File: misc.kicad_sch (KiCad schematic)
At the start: 0 parts

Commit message: [#56643] Create buses for interfaces, assign buses to blocks
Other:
- company: (none) -> Antmicro Ltd.
- title: (none) -> Com Express 7 baseboard
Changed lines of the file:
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@@
 (kicad_sch (version 20230121) (generator eeschema)
-  (paper "A4")
+  (paper "A3")
+  (title_block
+    (title "Com Express 7 baseboard")
+    (date "2024-03-22")
+    (rev "1.0.0")
+    (company "Antmicro Ltd.")
+  )
 )

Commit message: [#57905] Add ADT7476AARQZ temperature/voltage/fan system monitor, LEDs
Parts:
- added C135, C137, C138, C139, C140, C141, C142, C143, C144: C_100n_0402, antmicro-footprints:C_0402_1005Metric, symbol antmicroCapacitors0402:C_100n_0402
- added C136: C_10u_0402, antmicro-footprints:C_0402_1005Metric, symbol antmicroCapacitors0402:C_10u_0402
- added D19: LED_RGB_PLCC4_ASMB_MTB1_0A3A2, antmicro-footprints:PLCC4_3.2x2.8mm, symbol antmicroLEDIndicationDiscrete:LED_RGB_PLCC4_ASMB_MTB1_0A3A2
- added D20: LED_G_0603_LTST-C190GKT, antmicro-footprints:LED_0603_1608Metric_G, symbol antmicroLEDIndicationDiscrete:LED_G_0603_LTST-C190GKT
- added F1: PTC_3A_1210, antmicro-footprints:F_1210_3225Metric, symbol antmicroFuses:PTC_3A_1210
- added H4, H5: Lightpipe_Bivar_SLP3-300-250-F, antmicro-footprints:Mech_Lightpipe_Bivar_SLP3-300-250-F, symbol antmicroMechanicalParts:Lightpipe_Bivar_SLP3-300-250-F
- added J10, J11, J12: Molex_KK_1x4_0470531000, antmicro-footprints:Conn_Molex_KK_1x4_0470531000, symbol antmicroWire2BoardConnectors:Molex_KK_1x4_0470531000
- added Q3, Q4: MMBT3904LT1G, antmicro-footprints:SOT-23-3, symbol antmicroTransistorsBipolarSingle:MMBT3904LT1G
- added R241, R242, R247: R_0R_0402, antmicro-footprints:R_0402_1005Metric, symbol antmicroResistors0402:R_0R_0402
- added R243, R244, R245, R246: R_10k_0402, antmicro-footprints:R_0402_1005Metric, symbol antmicroResistors0402:R_10k_0402
- added R248, R249, R250: R_220R_0402, antmicro-footprints:R_0402_1005Metric, symbol antmicroResistors0402:R_220R_0402
- added R251: R_330R_0402, antmicro-footprints:R_0402_1005Metric, symbol antmicroResistors0402:R_330R_0402
- added TP71, TP72, TP73, TP74, TP75: TP_0.75mm_SMD, antmicro-footprints:TP_SMD_0.75mm, symbol antmicroTestPoints:TP_0.75mm_SMD
- added U36: ADT7476AARQZ, symbol antmicroTemperatureSensorsAnalogandDigitalOutput:ADT7476AARQZ
- added U37, U38, U39: NTS0102_TSSOP, antmicro-footprints:TSSOP-8_3x3mm_P0.65mm, symbol antmicroLogicTranslatorsLevelShifters:NTS0102_TSSOP
- added U40, U41: 74LVC1G157-Q100H_SOT457, antmicro-footprints:SC-74-6_1.5x2.9mm_P0.95mm, symbol antmicroInterfaceAnalogSwitchesMultiplexersDemultiplexers:74LVC1G157-Q100H_SOT4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
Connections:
- new net: R241.2, U36.20 (+5V_{IN})
- new net: TP71.1, U36.8 (GPIO3)
- new net: D19.2 (C_{G}), R249.2
- new net: TP74.1, U36.5 (GPIO0)
- new net: R242.2, U36.21 (+12V_{IN})
- new net: Q4.1 (B), Q4.3 (C), U36.18 (D1+)
- new net: Q4.2 (E), U36.17 (D1-)
- new net: TP73.1, U36.6 (GPIO1)
- new net: D19.1 (C_{R}), R251.2
- new net: Q3.2 (E), U36.15 (D2-)
- new net: Q3.1 (B), Q3.3 (C), U36.16 (D2+)
- new net: R247.1, U36.19 (GPIO4)
- new net: TP72.1, U36.7 (GPIO2)
- new net: TP75.1, U36.9 (TACH3)
- new net: D20.1, R248.1
- new net: D19.3 (C_{B}), R250.2
- new net +12V: F1.1, R242.1
- new net +3V3: C135.2, C138.2, C139.2, C141.2, C143.2, C144.2, R243.2, R244.2, R246.2, R248.2, U36.4 (VCC), U37.3 (VCC_{A}), U37.6 (OE), U38.3 (VCC_{A}), U38.6 (OE), U39.3 (VCC_{A}), U39.6 (OE), U40.5 (VCC), U41.5 (VCC)
- new net +5V: C137.2, C140.2, C142.2, D19.4 (A), R241.1, U37.7 (VCC_{B}), U38.7 (VCC_{B}), U39.7 (VCC_{B})
- new net FAN_12V: C136.2, F1.2, J10.2, J11.2, J12.2
- new net GND: C135.1, C136.1, C137.1, C138.1, C139.1, C140.1, C141.1, C142.1, C143.1, C144.1, D20.2, J10.1, J11.1, J12.1, R245.1, U36.3 (GND), U37.2 (GND), U38.2 (GND), U39.2 (GND), U40.2 (GND), U41.2 (GND)
- new net LED_B: R250.1
- new net LED_G: R249.1
- new net LED_R: R251.1
- new net PWM1: U36.24 (PWM1/XTO), U40.3 (I0)
- new net PWM2: U36.10 (PWM2/~{SMB_{ALERT}}), U41.3 (I0)
- new net PWM_{A3V3}: U37.4 (A_{2}), U40.4 (Y)
- new net PWM_{A5V}: J12.4, U37.1 (B_{2})
- new net PWM_{B3V3}: U38.4 (A_{2}), U41.4 (Y)
- new net PWM_{B5V}: J10.4, U38.1 (B_{2})
- new net PWM_{C5V}: J11.4, U39.1 (B_{2})
- new net PWM_{CPUFAN}: U39.4 (A_{2}), U40.1 (I1), U41.1 (I1)
- new net PWM_{SRCSEL}: R246.1, R247.2, U40.6 (S), U41.6 (S)
- new net SMBus.SCL: U36.2 (SCL)
- new net SMBus.SDA: U36.1 (SDA)
- new net TACH_{A3V3}: U36.11 (TACH1), U37.5 (A_{1})
- new net TACH_{A5V}: J12.3, U37.8 (B_{1})
- new net TACH_{B3V3}: U36.12 (TACH2), U38.5 (A_{1})
- new net TACH_{B5V}: J10.3, U38.8 (B_{1})
- new net TACH_{C5V}: J11.3, U39.8 (B_{1})
- new net TACH_{CPUFAN}: U39.5 (A_{1})
- new net ~{ADDREN}: R243.1, U36.13 (PWM3/~{ADDREN})
- new net ~{ADDRSEL}: R244.1, R245.2, U36.14 (TACH4/~{ADDR_{SEL}}/GPIO6)
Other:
- note added: "Boot LED"
- note added: "CASE FAN #1"
- note added: "CASE FAN #2"
- note added: "CPU FAN"
- note added: "Case fans can either share PWM speed control with CPU fan or be individually controlled from ADT7476AARQZ |PWM_{SRCSEL}| SOURCE | |0 | ADT7476 | |1 | CPU_{PWM} | It's high by default"
- note added: "Cold side temperature sensor"
- note added: "FAN CONNECTORS"
- note added: "FAN/VOLTAGE/TEMPERATURE MONITOR"
- note added: "FRONT PANEL LEDS"
- note added: "Hot side temperature sensor"
- note added: "Status LED"

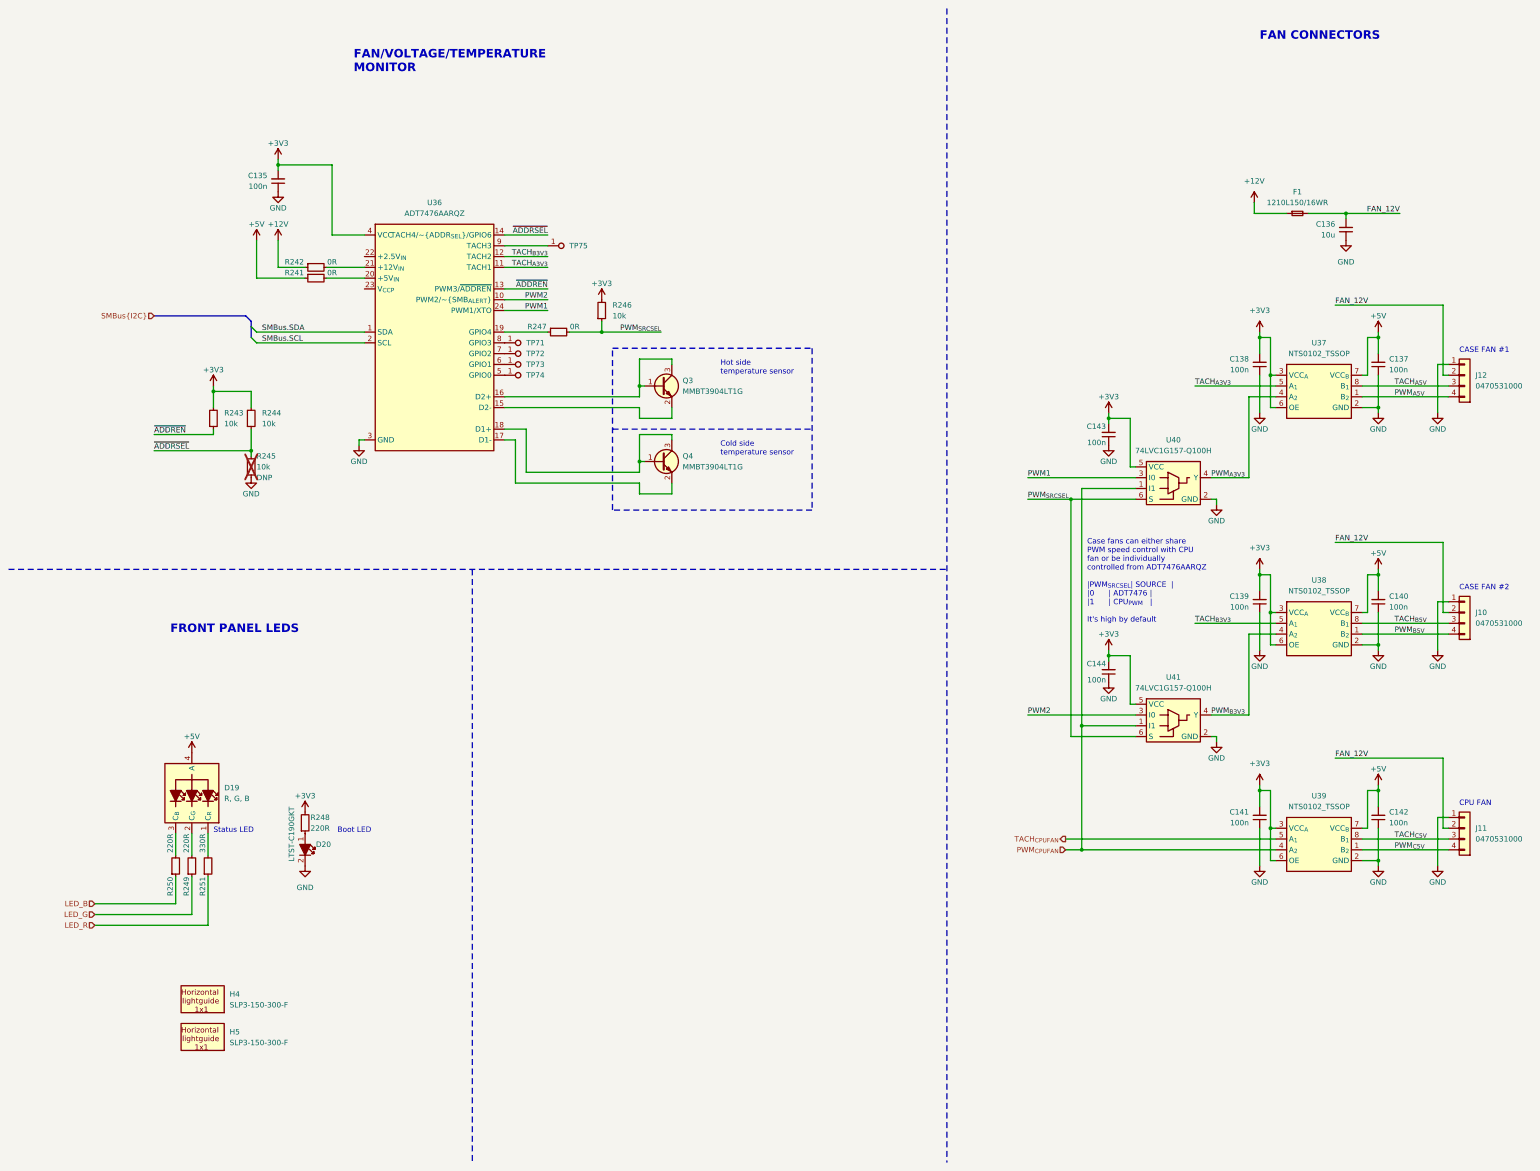
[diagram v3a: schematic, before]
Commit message: [#58137] Update backplane connector pinout
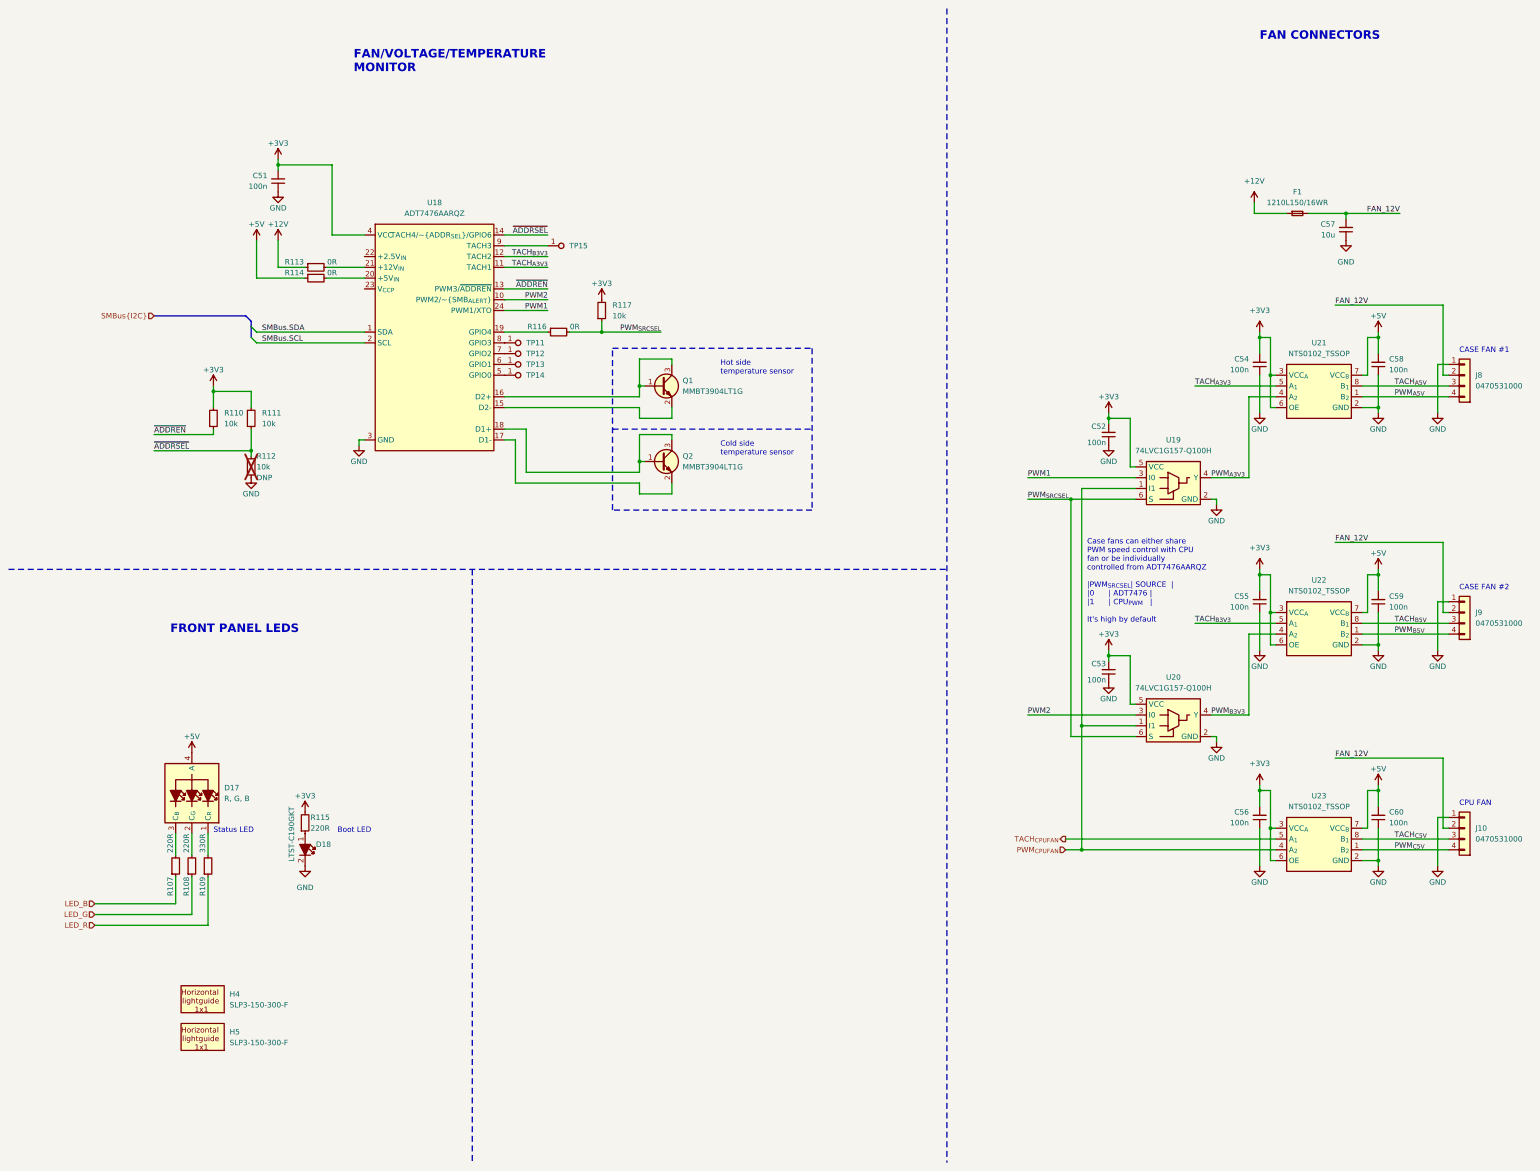
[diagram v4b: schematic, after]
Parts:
- renumbered C135 to C51, C143 to C52, C144 to C53, C138 to C54, C139 to C55, C141 to C56, C136 to C57, C137 to C58, C140 to C59, C142 to C60, D19 to D17, D20 to D18, J11 to J10, J12 to J8, J10 to J9, Q3 to Q1, Q4 to Q2, R250 to R107, R249 to R108, R251 to R109, R243 to R110, R244 to R111, R245 to R112, R242 to R113, R241 to R114, R248 to R115, R247 to R116, R246 to R117, TP71 to TP11, TP72 to TP12, TP73 to TP13, TP74 to TP14, TP75 to TP15, U36 to U18, U40 to U19, U41 to U20, U37 to U21, U38 to U22, U39 to U23

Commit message: Update symbols from the library
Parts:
- U18: footprint (none) -> antmicro-footprints:QSOP-24_8.65x6mm_P0.635mm; Author (none) -> Antmicro; License (none) -> Apache-2.0
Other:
- moved on the sheet: U18
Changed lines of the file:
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@@
       (effects (font (size 1.27 1.27)) hide)
     )
-    (property "Footprint" "" (at 96.52 66.04 0)
+    (property "Footprint" "antmicro-footprints:QSOP-24_8.65x6mm_P0.635mm" (at 96.52 66.04 0)
       (effects (font (size 1.27 1.27)) hide)
     )
@@
       (effects (font (size 1.27 1.27)) hide)
     )
+    (property "Author" "Antmicro" (at 144.78 83.82 0)
+      (effects (font (size 1.27 1.27) (thickness 0.15)) (justify left bottom) hide)
+    )
+    (property "License" "Apache-2.0" (at 144.78 86.36 0)
+      (effects (font (size 1.27 1.27) (thickness 0.15)) (justify left bottom) hide)
+    )
     (pin "5")

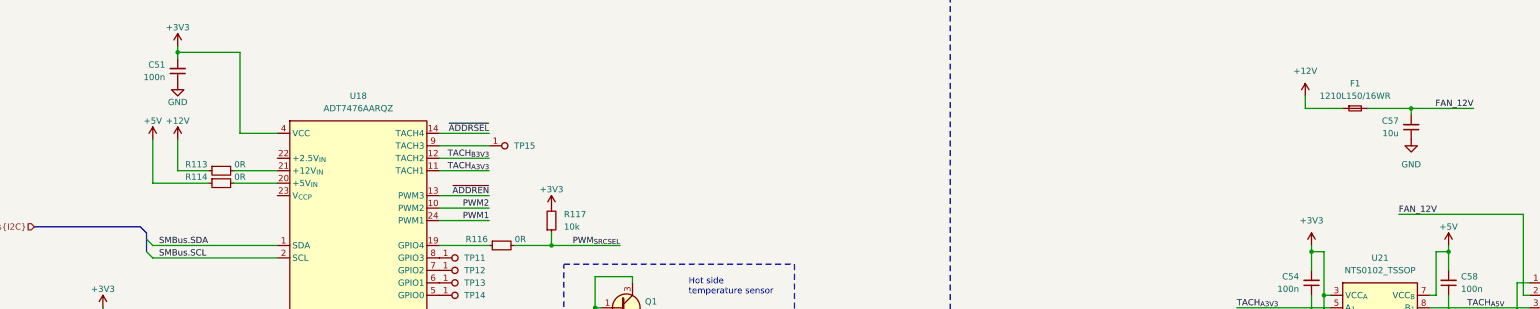
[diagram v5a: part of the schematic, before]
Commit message: [#58137] Add DC/DC supplies
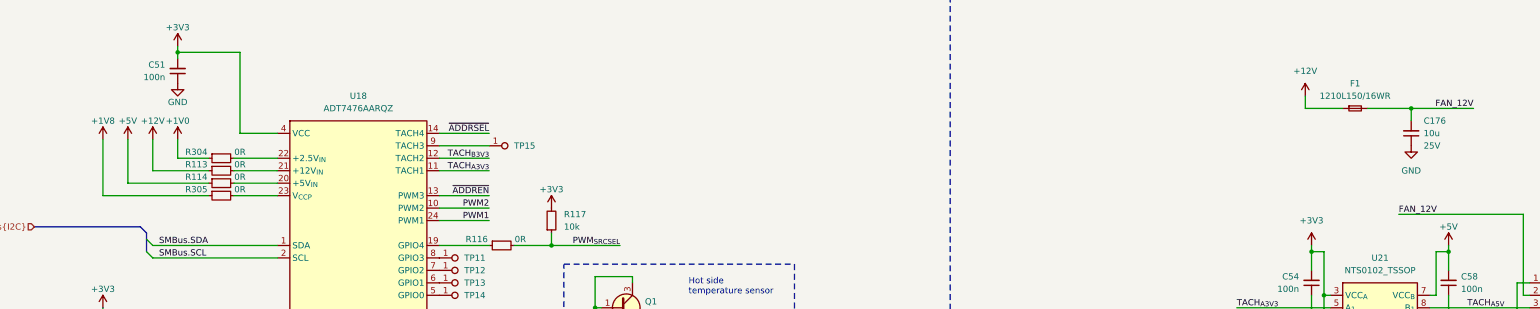
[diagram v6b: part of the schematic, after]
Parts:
- removed C57: C_10u_0402, antmicro-footprints:C_0402_1005Metric, symbol antmicroCapacitors0402:C_10u_0402
- added C176: C_10u_25V_0603, antmicro-footprints:C_0603_1608Metric, symbol antmicroCapacitors0603:C_10u_25V_0603
- added R304, R305: R_0R_0402, antmicro-footprints:R_0402_1005Metric, symbol antmicroResistors0402:R_0R_0402
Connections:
- net FAN_12V: now also C176.2
- net GND: now also C176.1
- net at U18.22 (+2.5V_{IN}): now also R304.2
- net at U18.23 (V_{CCP}): now also R305.2
- new net +1V0: R304.1
- new net +1V8: R305.1

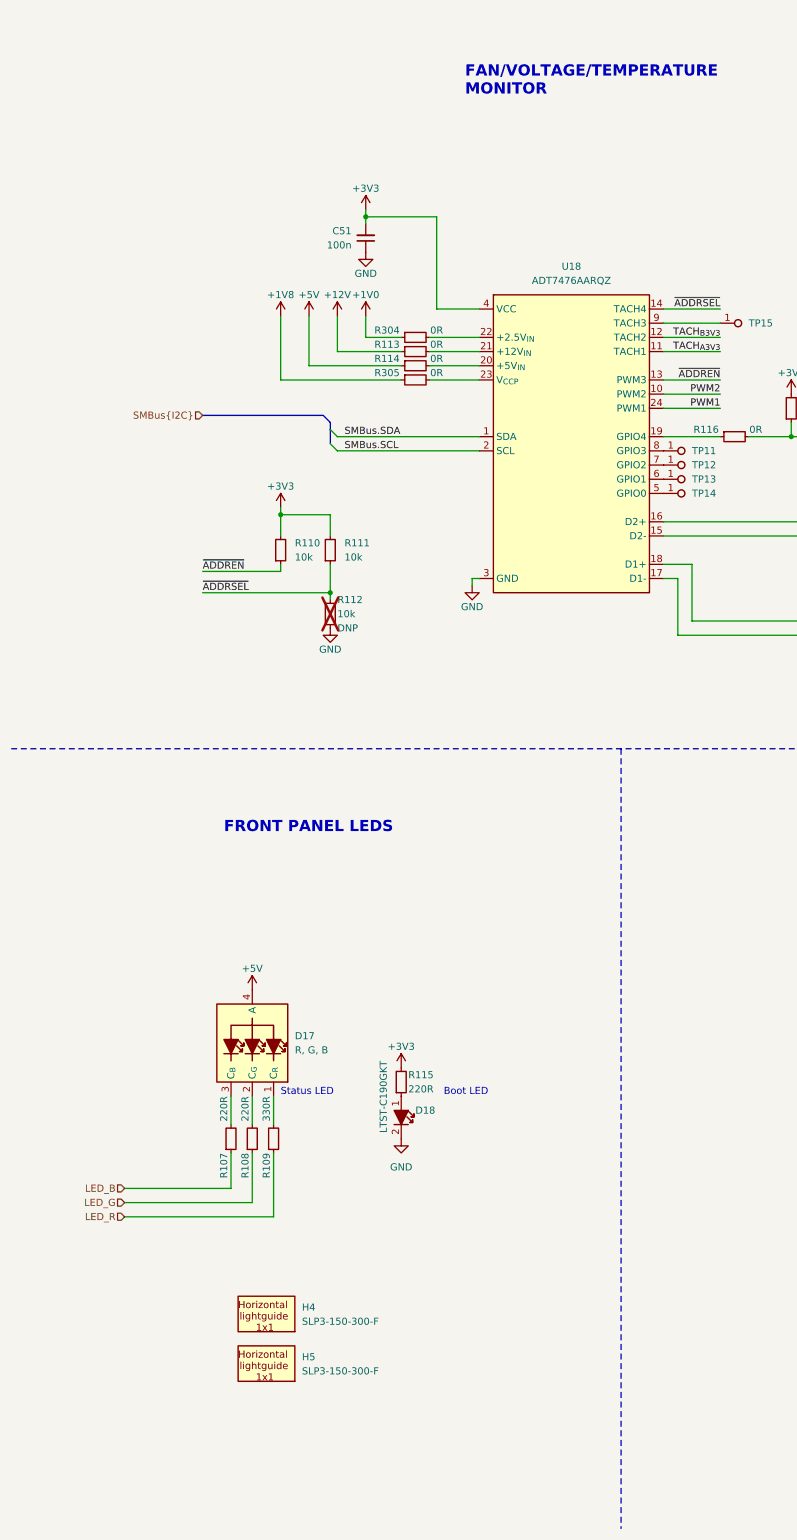
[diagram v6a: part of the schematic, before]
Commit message: [#58137] Add power sequencing and reset
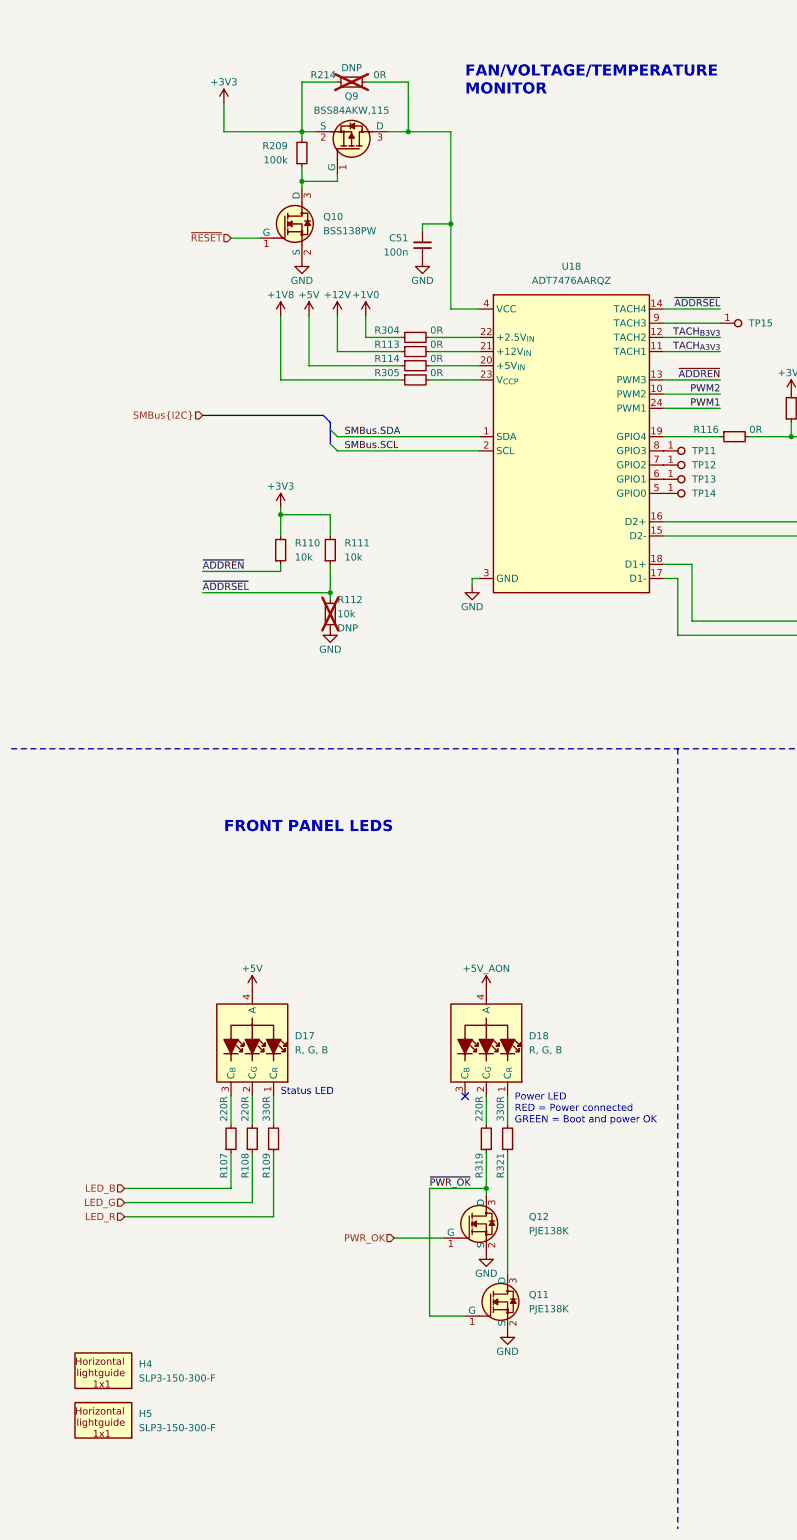
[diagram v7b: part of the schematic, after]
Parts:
- removed D18: LED_G_0603_LTST-C190GKT, antmicro-footprints:LED_0603_1608Metric_G, symbol antmicroLEDIndicationDiscrete:LED_G_0603_LTST-C190GKT
- removed R115: R_220R_0402, antmicro-footprints:R_0402_1005Metric, symbol antmicroResistors0402:R_220R_0402
- added D18: LED_RGB_PLCC4_ASMB_MTB1_0A3A2, antmicro-footprints:PLCC4_3.2x2.8mm, symbol antmicroLEDIndicationDiscrete:LED_RGB_PLCC4_ASMB_MTB1_0A3A2
- added Q10: BSS138PW, antmicro-footprints:SC70-3, symbol antmicroTransistorsFETsMOSFETsSingle:BSS138PW
- added Q11, Q12: PJE138K, antmicro-footprints:SOT-523, symbol antmicroTransistorsFETsMOSFETsSingle:PJE138K
- added Q9: BSS84AKW, antmicro-footprints:SOT-323, symbol antmicroTransistorsFETsMOSFETsSingle:BSS84AKW
- added R209: R_100k_0402, antmicro-footprints:R_0402_1005Metric, symbol antmicroResistors0402:R_100k_0402
- added R214: R_0R_0402, antmicro-footprints:R_0402_1005Metric, symbol antmicroResistors0402:R_0R_0402
- added R319: R_220R_0402, antmicro-footprints:R_0402_1005Metric, symbol antmicroResistors0402:R_220R_0402
- added R321: R_330R_0402, antmicro-footprints:R_0402_1005Metric, symbol antmicroResistors0402:R_330R_0402
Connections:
- net +3V3: now also Q9.2 (S), R209.2, R214.1; no longer C51.2, U18.4 (VCC)
- net GND: now also Q10.2 (S), Q11.2 (S), Q12.2 (S)
- new net: Q10.3 (D), Q9.1 (G), R209.1
- new net: C51.2, Q9.3 (D), R214.2, U18.4 (VCC)
- new net: Q11.3 (D), R321.1
- new net: D18.1 (C_{R}), R321.2
- new net: D18.2 (C_{G}), R319.2
- new net +5V_AON: D18.4 (A)
- new net PWR_OK: Q12.1 (G)
- new net ~{PWR_OK}: Q11.1 (G), Q12.3 (D), R319.1
- new net ~{RESET}: Q10.1 (G)
- no-connect marks 0 -> 1
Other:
- note added: "Power LED RED = Power connected GREEN = Boot and power OK"
- note removed: "Boot LED"
- moved on the sheet: C51, H4, H5
